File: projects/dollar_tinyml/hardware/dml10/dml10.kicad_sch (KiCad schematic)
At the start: 45 parts, among them J1 Conn_01x03, J2 USB_A, J3 Header 2.54mm, J4 Header 2.54mm, U1 CH32V003F4P6, U2 LTC4054ES5-4.2, U3 BM7161, U4 LM321, U5 LIS3DH

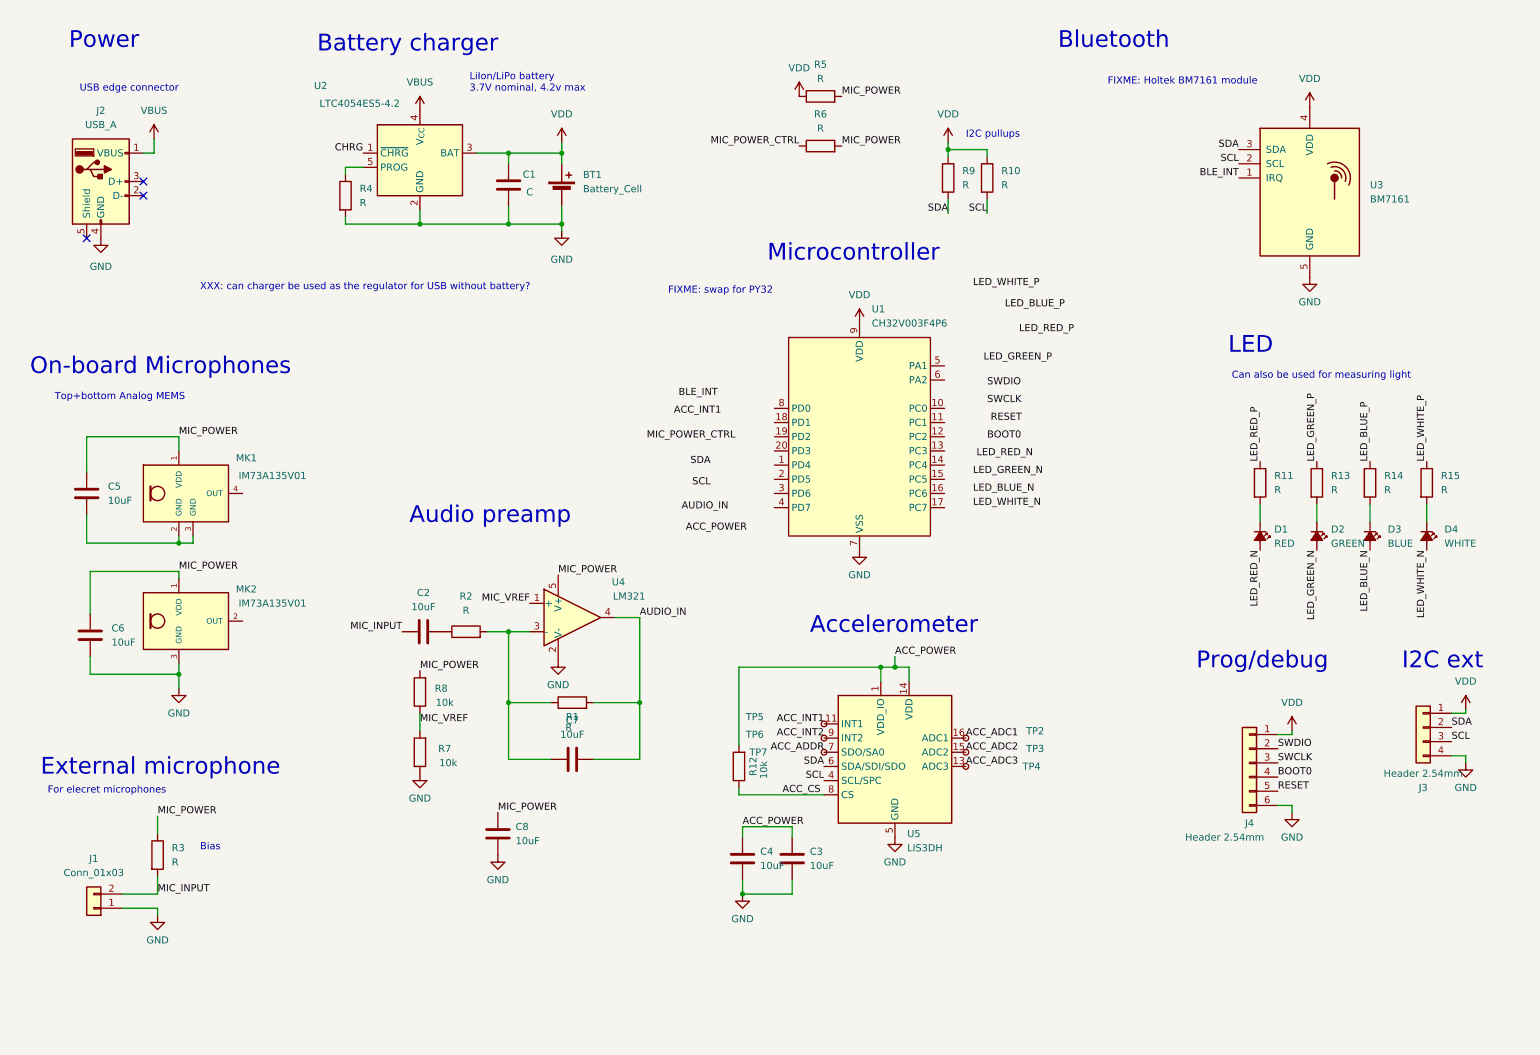
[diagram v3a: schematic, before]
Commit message: dollarml: Some fixes to schematic and layout
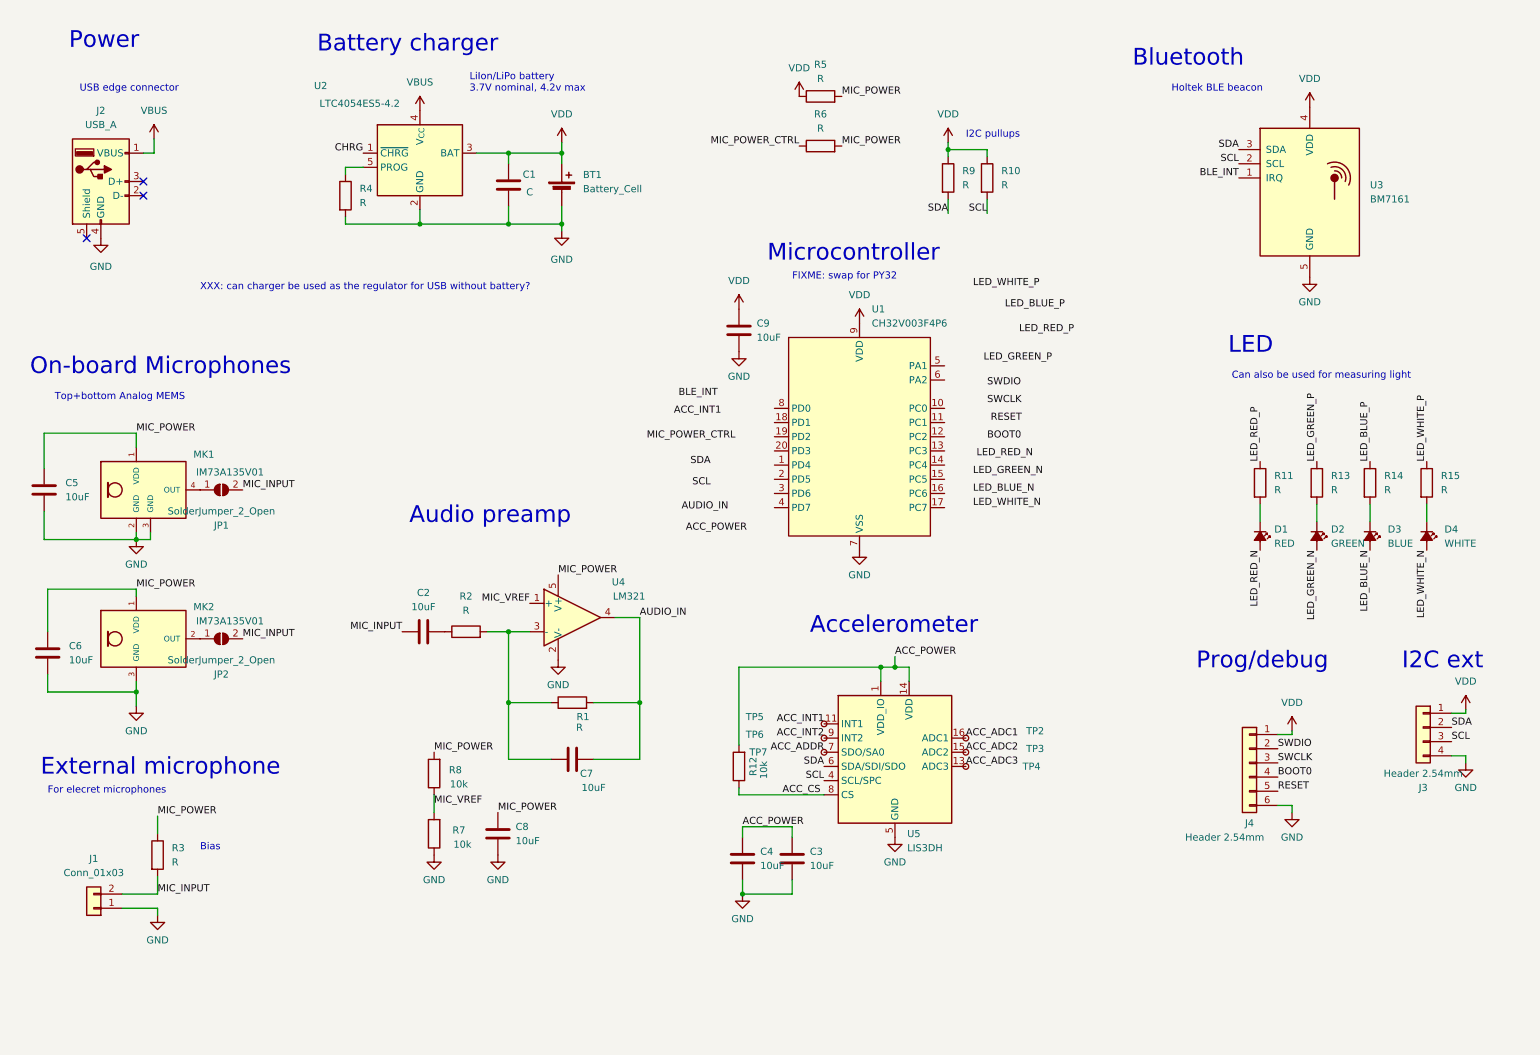
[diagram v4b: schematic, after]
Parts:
- added C9: 10uF, Capacitor_SMD:C_0603_1608Metric, symbol Device:C
- added JP1, JP2: SolderJumper_2_Open, Jumper:SolderJumper-2_P1.3mm_Open_RoundedPad1.0x1.5mm, symbol Jumper:SolderJumper_2_Open
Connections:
- net GND: now also C5.2, MK1.2 (GND), MK1.3 (GND), C9.1
- net MIC_INPUT: now also JP1.2 (B), JP2.2 (B)
- net VDD: now also C9.2
- net at MK1.4 (OUT): now also JP1.1 (A)
- net at MK2.2 (OUT): now also JP2.1 (A)
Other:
- note added: "Holtek BLE beacon"
- note removed: "FIXME: Holtek BM7161 module"
- moved on the sheet: C5, C6, MK1, MK2, R7, R8

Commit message: dollarml: Do most of layout and routing
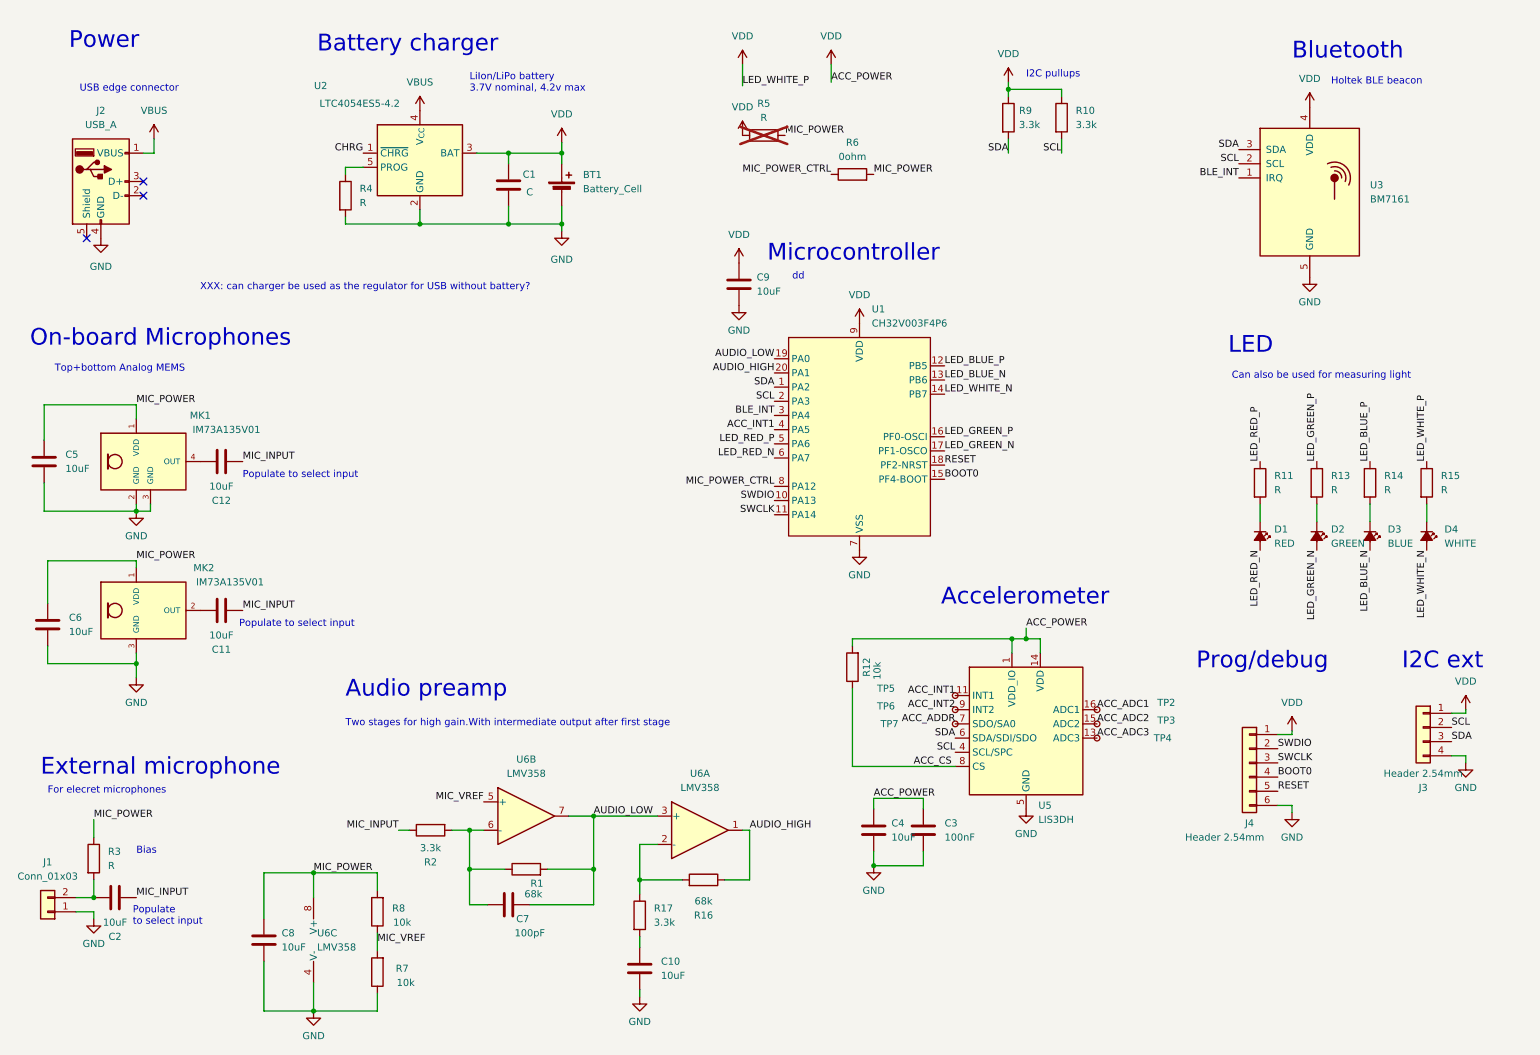
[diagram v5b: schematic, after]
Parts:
- removed JP1, JP2: SolderJumper_2_Open, Jumper:SolderJumper-2_P1.3mm_Open_RoundedPad1.0x1.5mm, symbol Jumper:SolderJumper_2_Open
- removed U4: LM321, Package_TO_SOT_SMD:SOT-23-5, symbol Amplifier_Operational:LM321
- added C10, C11, C12: 10uF, Capacitor_SMD:C_0603_1608Metric, symbol Device:C
- added R16: 68k, Resistor_SMD:R_0603_1608Metric, symbol Device:R
- added R17: 3.3k, Resistor_SMD:R_0603_1608Metric, symbol Device:R
- added U6: LMV358, Package_SO:MSOP-8_3x3mm_P0.65mm, symbol Amplifier_Operational:LMV358
- C3: value 10uF -> 100nF
- C7: value 10uF -> 100pF
- J1: footprint Connector_PinHeader_2.54mm:PinHeader_1x02_P2.54mm_Vertical -> Connector_PinHeader_1.27mm:PinHeader_1x02_P1.27mm_Horizontal
- R1: value R -> 68k
- R10, R2, R9: value R -> 3.3k
- R5: now not fitted
- R6: value R -> 0ohm
- U1: symbol wch-mcu:CH32V003F4P6 -> dml10:PY32F003F1xP
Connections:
- net ACC_POWER is gone; now on net VDD: C3.1, C4.1, R12.2, U5.1 (VDD_IO), U5.14 (VDD)
- net AUDIO_IN is gone; now on net AUDIO_LOW: C7.2, R1.2
- net LED_WHITE_P is gone; now on net VDD: R15.1
- net ACC_INT1: now also U1.4 (PA5)
- net BLE_INT: now also U1.3 (PA4)
- net BOOT0: now also U1.15 (PF4-BOOT)
- net GND: now also C10.2, U6.4 (V-)
- net LED_BLUE_N: now also U1.13 (PB6)
- net LED_BLUE_P: now also U1.12 (PB5)
- net LED_GREEN_N: now also U1.17 (PF1-OSCO)
- net LED_GREEN_P: now also U1.16 (PF0-OSCI)
- net LED_RED_N: now also U1.6 (PA7)
- net LED_RED_P: now also U1.5 (PA6)
- net LED_WHITE_N: now also U1.14 (PB7)
- net MIC_INPUT: now also C2.1, R2.1, C11.1, C12.1; no longer C2.2, J1.2 (Pin_2), R3.2
- net MIC_POWER: now also U6.8 (V+)
- net MIC_POWER_CTRL: now also U1.8 (PA12)
- net MIC_VREF: now also U6.5 (+)
- net RESET: now also U1.18 (PF2-NRST)
- net SCL: now also J3.2 (Pin_2), U1.2 (PA3); no longer J3.3 (Pin_3)
- net SDA: now also J3.3 (Pin_3), U1.1 (PA2); no longer J3.2 (Pin_2)
- net SWCLK: now also U1.11 (PA14)
- net SWDIO: now also U1.10 (PA13)
- net at MK1.4 (OUT): now also C12.2
- net at MK2.2 (OUT): now also C11.2
- net at C7.1, R1.1, R2.2: now also U6.6 (-)
- net AUDIO_LOW: now reaches U1.19 (PA0)
- net AUDIO_LOW: now also U6.3 (+), U6.7
- net AUDIO_HIGH: now reaches U1.20 (PA1)
- net AUDIO_HIGH: now also R16.1, U6.1
- new net: C2.2, J1.2 (Pin_2), R3.2
- new net: R16.2, R17.1, U6.2 (-)
- new net: C10.1, R17.2
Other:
- note added: "Populate to select input"
- note added: "Two stages for high gain.With intermediate output after first stage"
- note added: "dd"
- note removed: "FIXME: swap for PY32"
- moved on the sheet: C2, C3, C4, C5, C6, C7, C8, C9, J1, MK1, MK2, R1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

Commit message: dollarml: Fixup headers
Board outline is only thing missing now?
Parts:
- removed J3: Header 2.54mm, Connector_PinHeader_2.54mm:PinHeader_1x04_P2.54mm_Vertical, symbol Connector_Generic:Conn_01x04
- added H1: MountingHole, dml10:Mousebite_0.6mmX8, symbol Mechanical:MountingHole
- added J6: Conn_01x03, Connector_PinHeader_1.27mm:PinHeader_1x03_P1.27mm_Vertical, symbol Connector_Generic:Conn_01x03
- J4: footprint Connector_PinHeader_2.54mm:PinHeader_1x06_P2.54mm_Vertical -> Connector_PinHeader_2.54mm:PinHeader_1x14_P2.54mm_Vertical; symbol Connector_Generic:Conn_01x06 -> Connector_Generic:Conn_01x14
- U1: value CH32V003F4P6 -> PY32F003F16P6TU
- U2: value LTC4054ES5-4.2 -> LTC4054
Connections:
- net AUDIO_HIGH: now also J6.1 (Pin_1)
- net AUDIO_LOW: now also J6.2 (Pin_2)
- net BOOT0: now also J4.10 (Pin_10); no longer J4.4 (Pin_4)
- net GND: now also J4.14 (Pin_14), J4.3 (Pin_3), J4.7 (Pin_7), J6.3 (Pin_3); no longer J4.6 (Pin_6)
- net LED_BLUE_N: now also J4.13 (Pin_13)
- net LED_BLUE_P: now also J4.12 (Pin_12)
- net RESET: now also J4.11 (Pin_11); no longer J4.5 (Pin_5)
- net SCL: now also J4.4 (Pin_4)
- net SDA: now also J4.5 (Pin_5)
- net SWCLK: now also J4.9 (Pin_9); no longer J4.3 (Pin_3)
- net SWDIO: now also J4.8 (Pin_8); no longer J4.2 (Pin_2)
- net VBUS: now also J4.1 (Pin_1)
- net VDD: now also J4.2 (Pin_2), J4.6 (Pin_6); no longer J4.1 (Pin_1)
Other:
- note added: "Header"
- note removed: "I2C ext"
- note removed: "Prog/debug"
- moved on the sheet: D1, D2, D3, D4, R11, R13, R14, R15, U3
